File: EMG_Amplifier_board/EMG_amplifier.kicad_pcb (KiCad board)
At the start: 2 copper layers, 50 x 28 mm, 55 parts, among them J1 Conn_01x04_Socket, J2 Conn_01x04_Pin, J3 Conn_01x06_Pin, J4 Conn_01x06_Socket, J7 Conn_01x06_Pin, U1 LPV821DBVR, U2 INA333xxDGK, U3 LPV821DBVR, U5 LPV821DBVR, U6 LPV821DBVR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

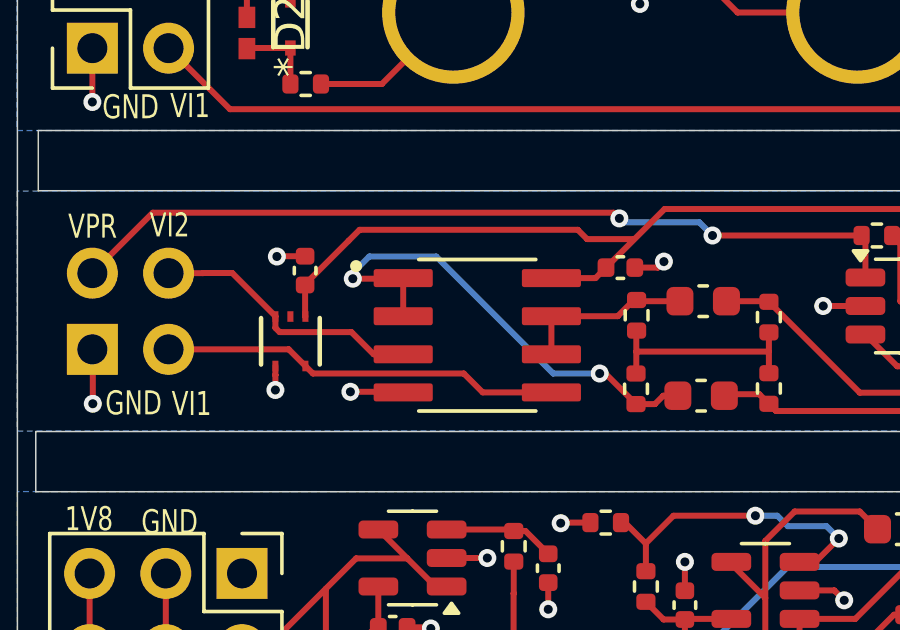
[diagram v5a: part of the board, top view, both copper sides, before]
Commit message: add buck converter 3v3 to 1v8, start new two-board sigacq project
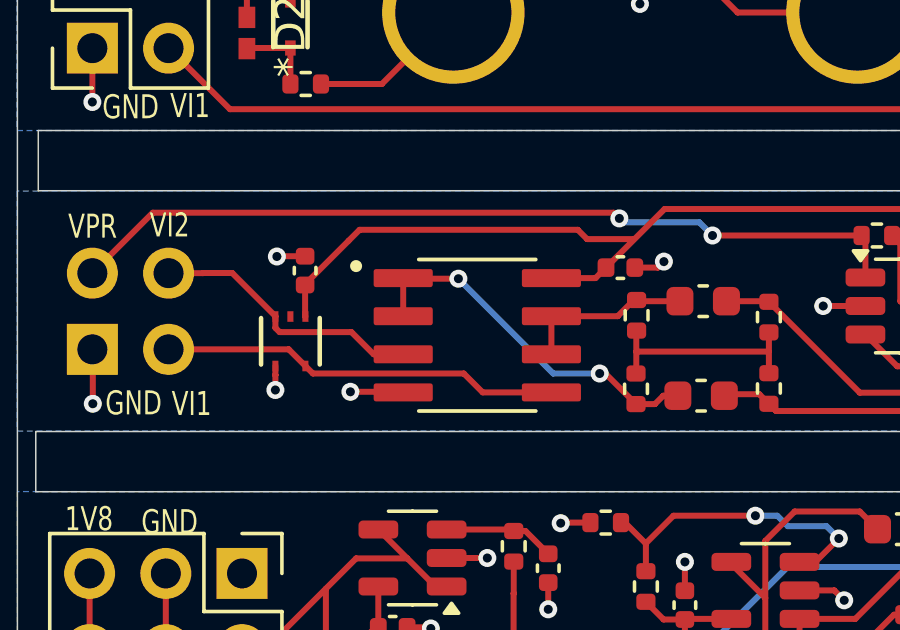
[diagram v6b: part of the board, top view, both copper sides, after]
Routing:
- net Net-(U8--INA): track 16.4 -> 12.3 mm
- added copper zone on In1.Cu, net GND
- added copper zone on In2.Cu, net GND
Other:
- copper layers 2 -> 4
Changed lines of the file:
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@@
 	(layers
 		(0 "F.Cu" signal)
+		(1 "In1.Cu" signal)
+		(2 "In2.Cu" signal)
 		(31 "B.Cu" signal)
 		(32 "B.Adhes" user "B.Adhesive")
@@
 	)
 	(setup
+		(stackup
+			(layer "F.SilkS"
+				(type "Top Silk Screen")
+			)
+			(layer "F.Paste"
+				(type "Top Solder Paste")
+			)
+			(layer "F.Mask"
+				(type "Top Solder Mask")
+				(thickness 0.01)
+			)
+			(layer "F.Cu"
+				(type "copper")
+				(thickness 0.035)
+			)
+			(layer "dielectric 1"
+				(type "prepreg")
+				(thickness 0.1)
+				(material "FR4")
+				(epsilon_r 4.5)
+				(loss_tangent 0.02)
+			)
+			(layer "In1.Cu"
+				(type "copper")
+				(thickness 0.035)
+			)
+			(layer "dielectric 2"
+				(type "core")
+				(thickness 1.24)
+				(material "FR4")
+				(epsilon_r 4.5)
+				(loss_tangent 0.02)
+			)
+			(layer "In2.Cu"
+				(type "copper")
+				(thickness 0.035)
+			)
+			(layer "dielectric 3"
+				(type "prepreg")
+				(thickness 0.1)
+				(material "FR4")
+				(epsilon_r 4.5)
+				(loss_tangent 0.02)
+			)
+			(layer "B.Cu"
+				(type "copper")
+				(thickness 0.035)
+			)
+			(layer "B.Mask"
+				(type "Bottom Solder Mask")
+				(thickness 0.01)
+			)
+			(layer "B.Paste"
+				(type "Bottom Solder Paste")
+			)
+			(layer "B.SilkS"
+				(type "Bottom Silk Screen")
+			)
+			(copper_finish "None")
+			(dielectric_constraints no)
+		)
 		(pad_to_mask_clearance 0)
 		(allow_soldermask_bridges_in_footprints no)
@@
 		(tags "capacitor")
 		(property "Reference" "C22"
-			(at 0 -1.16 -90)
+			(at 0 -1.16 90)
 			(layer "F.SilkS")
 			(hide yes)
@@
 		)
 		(property "Value" "0.1uF"
-			(at 0 1.16 -90)
+			(at 0 1.16 90)
 			(layer "F.Fab")
 			(hide yes)
@@
 		)
 		(fp_text user "${REFERENCE}"
-			(at 0 0 -90)
+			(at 0 0 90)
 			(layer "F.Fab")
 			(effects
@@
 		(tags "capacitor")
 		(property "Reference" "C20"
-			(at 0 -1.16 180)
+			(at 0 -1.16 0)
 			(layer "F.SilkS")
 			(hide yes)
@@
 		)
 		(property "Value" "0.1uF"
-			(at 0 1.16 180)
+			(at 0 1.16 0)
 			(layer "F.Fab")
 			(hide yes)
@@
 		)
 		(fp_text user "${REFERENCE}"
-			(at 0 0 180)
+			(at 0 0 0)
 			(layer "F.Fab")
 			(effects
@@
 	)
 	(segment
+		(start 26.7 24.94)
+		(end 24.88 24.94)
+		(width 0.2)
+		(layer "F.Cu")
+		(net 32)
+	)
+	(segment
 		(start 31.6 28.1)
 		(end 32.62 29.12)
@@
 	)
 	(segment
-		(start 31.41 28.1)
-		(end 31.6 28.1)
+		(start 24.88 24.94)
+		(end 24.86 24.92)
 		(width 0.2)
 		(layer "F.Cu")
@@
 	)
 	(segment
-		(start 33.25 29.12)
-		(end 33.53 28.84)
+		(start 31.41 28.1)
+		(end 31.6 28.1)
 		(width 0.2)
 		(layer "F.Cu")
@@
 	)
 	(segment
-		(start 23.18 24.94)
-		(end 24.84 24.94)
+		(start 33.25 29.12)
+		(end 33.53 28.84)
 		(width 0.2)
 		(layer "F.Cu")
@@
 	)
 	(via
-		(at 23.18 24.94)
+		(at 31.41 28.1)
 		(size 0.6)
 		(drill 0.3)
@@
 	)
 	(via
-		(at 31.41 28.1)
+		(at 26.7 24.94)
 		(size 0.6)
 		(drill 0.3)
@@
 	)
 	(segment
-		(start 23.73 24.2)
-		(end 25.96 24.2)
-		(width 0.2)
-		(layer "B.Cu")
-		(net 32)
-	)
-	(segment
-		(start 29.86 28.1)
-		(end 31.41 28.1)
+		(start 26.75 24.99)
+		(end 26.7 24.94)
 		(width 0.2)
 		(layer "B.Cu")
@@
 	)
 	(segment
-		(start 23.18 24.75)
-		(end 23.73 24.2)
-		(width 0.2)
-		(layer "B.Cu")
-		(net 32)
-	)
-	(segment
-		(start 23.18 24.94)
-		(end 23.18 24.75)
+		(start 26.75 24.99)
+		(end 29.86 28.1)
 		(width 0.2)
 		(layer "B.Cu")
@@
 	)
 	(segment
-		(start 25.96 24.2)
-		(end 29.86 28.1)
+		(start 29.86 28.1)
+		(end 31.41 28.1)
 		(width 0.2)
 		(layer "B.Cu")
@@
 	)
 	(zone
+		(net 1)
+		(net_name "GND")
+		(layers "In1.Cu" "In2.Cu")
+		(hatch edge 0.5)
+		(priority 3)
+		(connect_pads
+			(clearance 0.5)
+		)
+		(min_thickness 0.25)
+		(filled_areas_thickness no)
+		(fill yes
+			(thermal_gap 0.5)
+			(thermal_bridge_width 0.5)
+		)
+		(polygon
+			(pts
+				(xy 12 32.04) (xy 12 40.03) (xy 61.97 40.03) (xy 61.97 32.03)
+			)
+		)
+	)
+	(zone
